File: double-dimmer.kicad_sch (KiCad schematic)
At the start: 8 parts, among them J1 Netzspannung, J2 Screw_Terminal_01x05, J3 Conn_01x04, SW1 SW_Push, SW2 SW_Push

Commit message: Added switches to layout and do routing
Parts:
- SW1, SW2: footprint (none) -> pts636:pts636
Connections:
- net L_OUT2: now reaches J2.3 (Pin_3), U2.3 (L_OUT)
- net N_OUT2: now reaches J2.2 (Pin_2), U2.4 (N_OUT)
- net N_OUT1: now reaches J2.4 (Pin_4), U1.4 (N_OUT)
- net L_OUT1: now reaches J2.5 (Pin_5), U1.3 (L_OUT)
- net L_Prefuse: now reaches F1.1, J1.3 (Pin_3)
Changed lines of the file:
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@@
     (stroke (width 0) (type default))
   )
+  (global_label "L_OUT1" (shape input) (at 86.36 72.39 90) (fields_autoplaced)
+    (effects (font (size 1.27 1.27)) (justify left))
+    (property "Intersheetrefs" "${INTERSHEET_REFS}" (at 86.36 62.571 90)
+      (effects (font (size 1.27 1.27)) (justify left) hide)
+    )
+  )
   (global_label "Switch_B2" (shape input) (at 36.83 101.6 0) (fields_autoplaced)
     (effects (font (size 1.27 1.27)) (justify left))
@@
     )
   )
+  (global_label "N_OUT2" (shape input) (at 88.9 95.25 90) (fields_autoplaced)
+    (effects (font (size 1.27 1.27)) (justify left))
+    (property "Intersheetrefs" "${INTERSHEET_REFS}" (at 88.9 85.1286 90)
+      (effects (font (size 1.27 1.27)) (justify left) hide)
+    )
+  )
+  (global_label "L_Prefuse" (shape input) (at 29.21 62.23 90) (fields_autoplaced)
+    (effects (font (size 1.27 1.27)) (justify left))
+    (property "Intersheetrefs" "${INTERSHEET_REFS}" (at 29.21 50.1129 90)
+      (effects (font (size 1.27 1.27)) (justify left) hide)
+    )
+  )
   (global_label "Switch_B1" (shape input) (at 62.23 83.82 180) (fields_autoplaced)
     (effects (font (size 1.27 1.27)) (justify right))
@@
     )
   )
+  (global_label "L_OUT2" (shape input) (at 86.36 92.71 90) (fields_autoplaced)
+    (effects (font (size 1.27 1.27)) (justify left))
+    (property "Intersheetrefs" "${INTERSHEET_REFS}" (at 86.36 82.891 90)
+      (effects (font (size 1.27 1.27)) (justify left) hide)
+    )
+  )
   (global_label "Switch_A2" (shape input) (at 106.68 104.14 180) (fields_autoplaced)
     (effects (font (size 1.27 1.27)) (justify right))
@@
     (property "Intersheetrefs" "${INTERSHEET_REFS}" (at 58.2167 72.39 0)
       (effects (font (size 1.27 1.27)) (justify right) hide)
+    )
+  )
+  (global_label "N_OUT1" (shape input) (at 88.9 74.93 90) (fields_autoplaced)
+    (effects (font (size 1.27 1.27)) (justify left))
+    (property "Intersheetrefs" "${INTERSHEET_REFS}" (at 88.9 64.8086 90)
+      (effects (font (size 1.27 1.27)) (justify left) hide)
     )
   )
@@
       (effects (font (size 1.27 1.27)))
     )
-    (property "Footprint" "" (at 31.75 96.52 0)
+    (property "Footprint" "pts636:pts636" (at 31.75 96.52 0)
       (effects (font (size 1.27 1.27)) hide)
     )
@@
       (effects (font (size 1.27 1.27)))
     )
-    (property "Footprint" "" (at 31.75 78.74 0)
-      (effects (font (size 1.27 1.27)) hide)
-    )
+    (property "Footprint" "pts636:pts636" (at 31.75 78.74 0)
+      (effects (font (size 1.27 1.27)) hide)
+    )

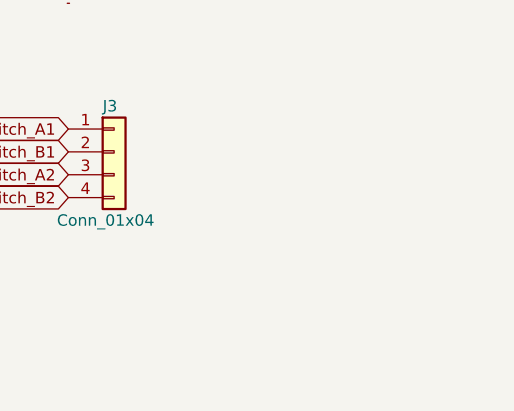
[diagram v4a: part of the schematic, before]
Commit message: Add mounting holes
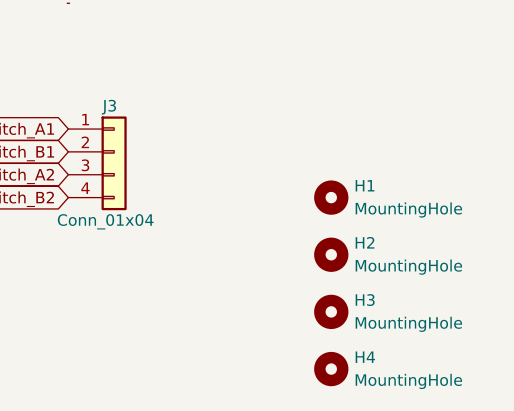
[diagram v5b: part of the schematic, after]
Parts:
- added H1, H2, H3, H4: MountingHole, MountingHole:MountingHole_3.2mm_M3, symbol Mechanical:MountingHole
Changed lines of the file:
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@@
+    )
+  )
+  (symbol (lib_id "Mechanical:MountingHole") (at 135.89 119.38 0) (unit 1)
+    (in_bom yes) (on_board yes) (dnp no) (fields_autoplaced)
+    (property "Reference" "H3" (at 138.43 118.11 0)
+      (effects (font (size 1.27 1.27)) (justify left))
+    )
+    (property "Value" "MountingHole" (at 138.43 120.65 0)
+      (effects (font (size 1.27 1.27)) (justify left))
+    )
+    (property "Footprint" "MountingHole:MountingHole_3.2mm_M3" (at 135.89 119.38 0)
+      (effects (font (size 1.27 1.27)) hide)
+    )
+    (property "Datasheet" "~" (at 135.89 119.38 0)
+      (effects (font (size 1.27 1.27)) hide)
+    )
+    (instances
+      (project "double-dimmer"
+        (path "/a2cfefb5-9b8f-4ea6-9600-ced2f5c1dc62"
+          (reference "H3") (unit 1)
+        )
+      )
     )
   )
@@
     )
   )
+  (symbol (lib_id "Mechanical:MountingHole") (at 135.89 125.73 0) (unit 1)
+    (in_bom yes) (on_board yes) (dnp no) (fields_autoplaced)
+    (property "Reference" "H4" (at 138.43 124.46 0)
+      (effects (font (size 1.27 1.27)) (justify left))
+    )
+    (property "Value" "MountingHole" (at 138.43 127 0)
+      (effects (font (size 1.27 1.27)) (justify left))
+    )
+    (property "Footprint" "MountingHole:MountingHole_3.2mm_M3" (at 135.89 125.73 0)
+      (effects (font (size 1.27 1.27)) hide)
+    )
+    (property "Datasheet" "~" (at 135.89 125.73 0)
+      (effects (font (size 1.27 1.27)) hide)
+    )
+    (instances
+      (project "double-dimmer"
+        (path "/a2cfefb5-9b8f-4ea6-9600-ced2f5c1dc62"
+          (reference "H4") (unit 1)
+        )
+      )
+    )
+  )
   (symbol (lib_id "Device:Fuse") (at 33.02 62.23 90) (unit 1)
     (in_bom yes) (on_board yes) (dnp no) (fields_autoplaced)
@@
         )
       )
+    )
+  )
+  (symbol (lib_id "Mechanical:MountingHole") (at 135.89 113.03 0) (unit 1)
+    (in_bom yes) (on_board yes) (dnp no) (fields_autoplaced)
+    (property "Reference" "H2" (at 138.43 111.76 0)
+      (effects (font (size 1.27 1.27)) (justify left))
+    )
+    (property "Value" "MountingHole" (at 138.43 114.3 0)
+      (effects (font (size 1.27 1.27)) (justify left))
+    )
+    (property "Footprint" "MountingHole:MountingHole_3.2mm_M3" (at 135.89 113.03 0)
+      (effects (font (size 1.27 1.27)) hide)
+    )
+    (property "Datasheet" "~" (at 135.89 113.03 0)
+      (effects (font (size 1.27 1.27)) hide)
+    )
+    (instances
+      (project "double-dimmer"
+        (path "/a2cfefb5-9b8f-4ea6-9600-ced2f5c1dc62"
+          (reference "H2") (unit 1)
+        )
+      )
+    )
+  )
+  (symbol (lib_id "Mechanical:MountingHole") (at 135.89 106.68 0) (unit 1)
+    (in_bom yes) (on_board yes) (dnp no) (fields_autoplaced)
+    (property "Reference" "H1" (at 138.43 105.41 0)
+      (effects (font (size 1.27 1.27)) (justify left))
+    )
+    (property "Value" "MountingHole" (at 138.43 107.95 0)
+      (effects (font (size 1.27 1.27)) (justify left))
+    )
+    (property "Footprint" "MountingHole:MountingHole_3.2mm_M3" (at 135.89 106.68 0)
+      (effects (font (size 1.27 1.27)) hide)
+    )
+    (property "Datasheet" "~" (at 135.89 106.68 0)
+      (effects (font (size 1.27 1.27)) hide)
+    )
+    (instances
+      (project "double-dimmer"
+        (path "/a2cfefb5-9b8f-4ea6-9600-ced2f5c1dc62"
+          (reference "H1") (unit 1)
+        )
+      )
